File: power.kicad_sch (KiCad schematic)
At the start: 34 parts, among them J1 Batt_conn_3p, J2 USB_C_Receptacle_PowerOnly_6P, J3 Conn_01x03_Pin, Q1 DTC143Z, U1 BQ24073RGTR, U2 TPD1E10B06DPYR, U3 TPD1E10B06DPYR, U4 TPD1E10B06DPYR, U5 TPS61022RWUR, U7 AP2112K-1.8

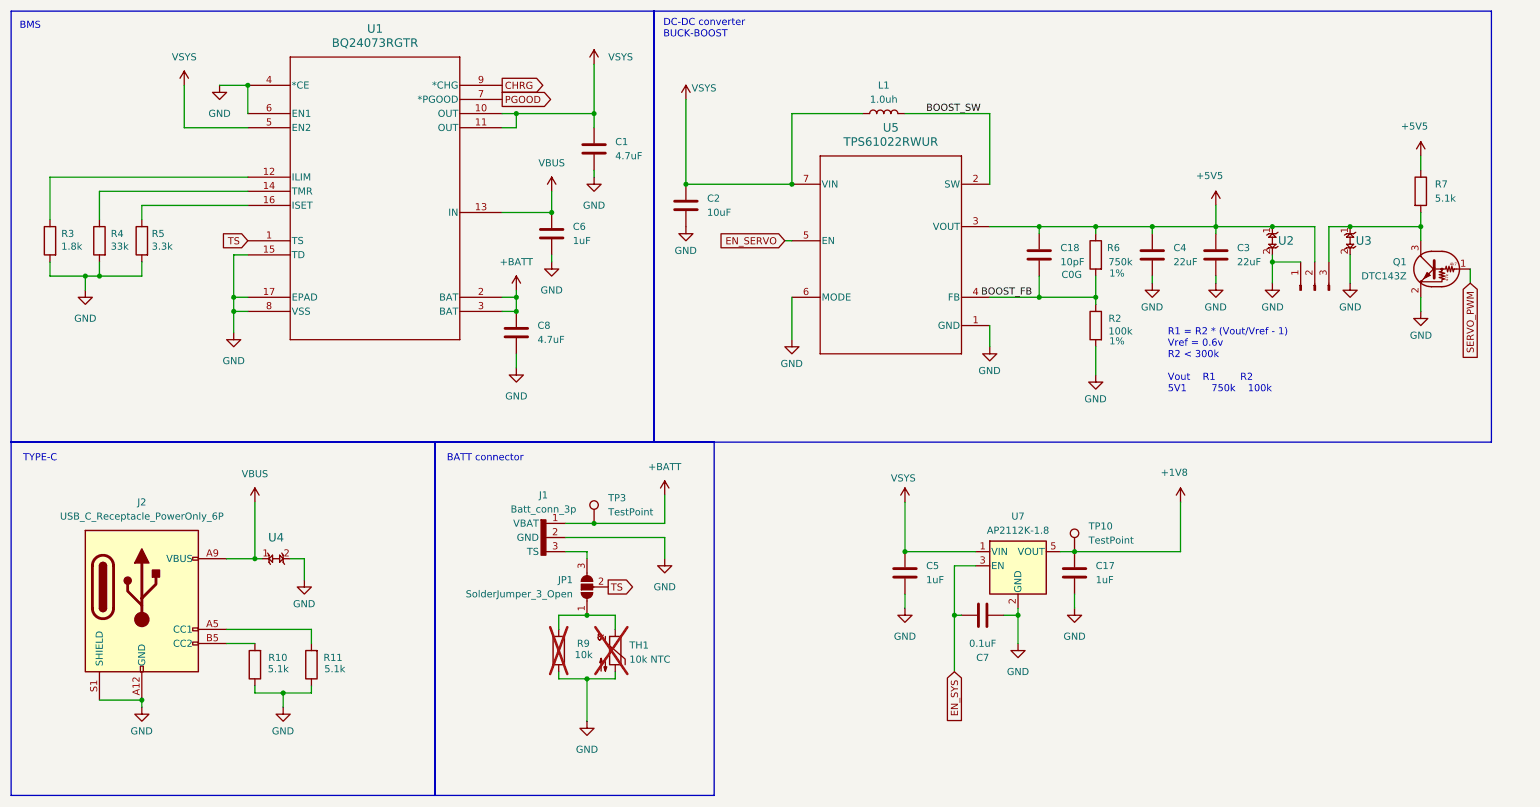
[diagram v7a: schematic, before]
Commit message: Updated schematics. Calculated inductor values
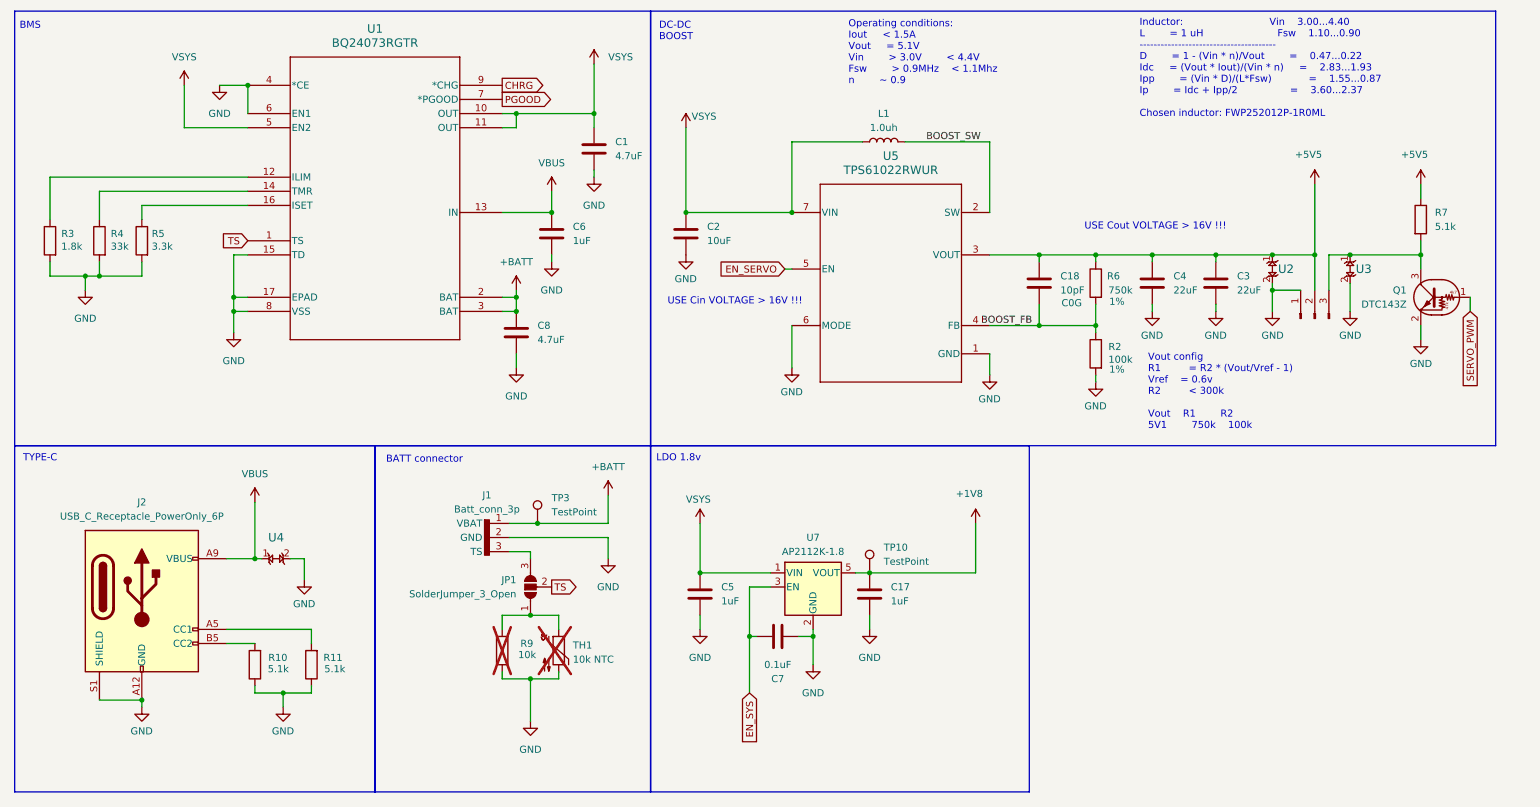
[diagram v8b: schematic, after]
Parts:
- L1: LCSC C5179457 -> C5179444
- R2: Tolerance (none) -> 1%; Tolerance  1% -> (none)
- U7: LCSC (none) -> C176944
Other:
- note added: "DC-DC BOOST"
- note added: "Inductor: Vin 3.00...4.40 L = 1 uH Fsw 1.10...0.90 --------------------------------------- D = 1 - (Vin * n)/Vout = 0.47...0.22 Idc = (Vout * Iout)/(Vin * n) = 2.83...1.93 Ipp = (Vin * D)/(L*Fsw) = 1.55...0.87 Ip = Idc + Ipp/2 = 3.60...2.37 Chosen inductor: FWP252012P-1R0ML"
- note added: "LDO 1.8v"
- note added: "Operating conditions: Iout < 1.5A Vout = 5.1V Vin > 3.0V < 4.4V Fsw > 0.9MHz < 1.1Mhz n ~ 0.9"
- note added: "USE Cin VOLTAGE > 16V !!!"
- note added: "USE Cout VOLTAGE > 16V !!!"
- note added: "Vout config R1 = R2 * (Vout/Vref - 1) Vref = 0.6v R2 < 300k Vout R1 R2 5V1 750k 100k"
- note removed: "DC-DC converter BUCK-BOOST"
- note removed: "R1 = R2 * (Vout/Vref - 1) Vref = 0.6v R2 < 300k Vout R1 R2 5V1 750k 100k"
- moved on the sheet: C17, C18, C2, C3, C4, C5, C7, J1, JP1, L1, Q1, R2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
